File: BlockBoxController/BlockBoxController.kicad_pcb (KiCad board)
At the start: 4 copper layers, 80.5 x 40 mm, 92 parts, among them J1 B1_SWLED, J10 I2C1/USART1, J11 I2C4/UART4, J12 B1_LED_BRIGHTNESS, J13 I2C5, J14 B1_BTN, J15 PWR, J2 SWD, J3 NHD-3.5-320240FT-CON, J4 CHG, J5 AMP, J6 I2S, J7 B1_LCD_SWITCH, J8 LED, J9 B1_LEDMODE, Q1 NX138BK, Q2 NX138BK, Q3 DMG2302UK, Q4 DMG2302UK, Q5 DMG2302UK, Q6 DMG2302UK, U1 STM32H725VGTx

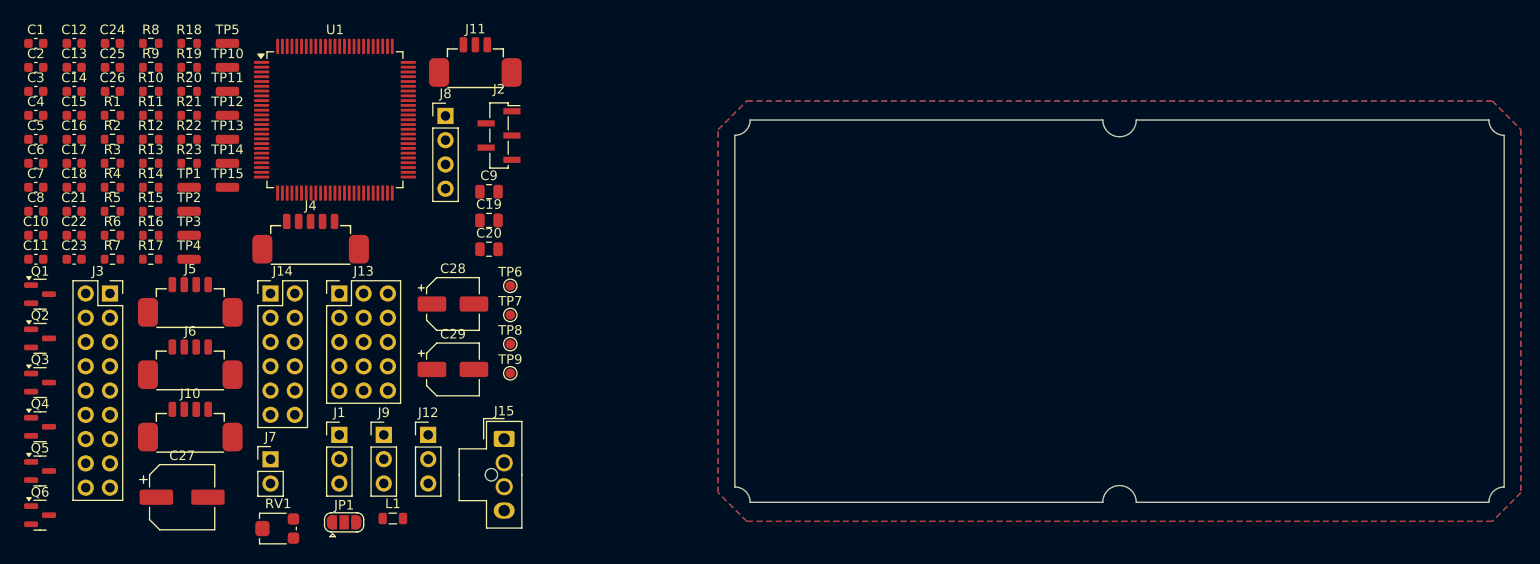
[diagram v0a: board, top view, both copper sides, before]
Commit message: BlockBoxController design done
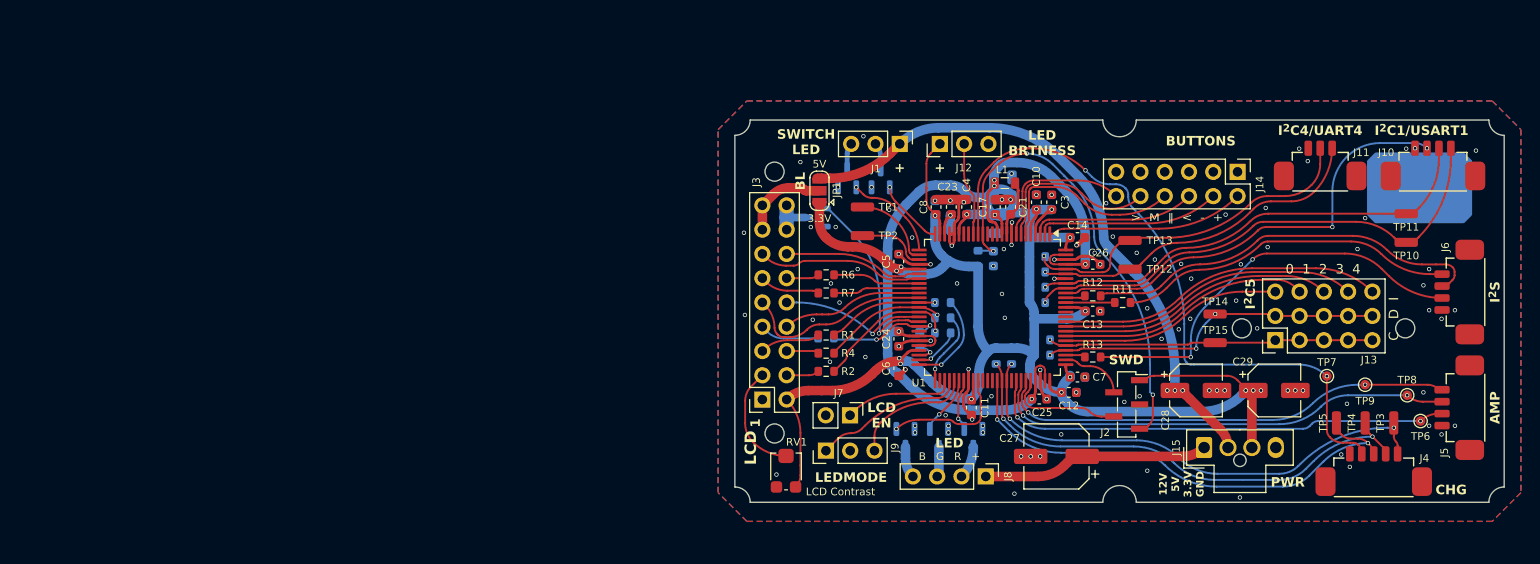
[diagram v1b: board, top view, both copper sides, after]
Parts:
- added REF**: Hole_2mm, BW_PassiveMechanical:Hole_2mm, F.Cu at (113.9, 85.4)
- added REF**: Hole_2mm, BW_PassiveMechanical:Hole_2mm, F.Cu at (179.9, 101.8)
- added REF**: Hole_2mm, BW_PassiveMechanical:Hole_2mm, F.Cu at (162.8, 101.8)
- added REF**: Hole_2mm, BW_PassiveMechanical:Hole_2mm, F.Cu at (113.9, 112.8)
- added REF**: BW_Logo_10x6.4mm, BW_Logo:BW_Logo_10x6.4mm, B.Cu at (181.4, 87.1)
- C1, C15, C16, C18, C19, C2, C20, C22, C9, Q1, Q2, Q3, Q4, Q5, Q6, R10, R14, R15, R16, R17, R18, R19, R20, R21, R22, R23, R3, R5, R8, R9: moved to B.Cu
- moved J5 133.8 mm to (186.2, 110.1), turned to 90 degrees
- moved J6 133.7 mm to (186.2, 98.0), turned to 90 degrees
- moved J10 132.9 mm to (182.8, 85.4)
- moved TP3 127.6 mm to (178.7, 111.7), turned to -90 degrees
- moved TP10 124.7 mm to (180.0, 92.8), turned to 180 degrees
- moved TP4 124.2 mm to (175.7, 111.7), turned to -90 degrees
- moved TP11 124.0 mm to (180.0, 89.8), turned to 180 degrees
- moved TP5 122.7 mm to (172.7, 111.7), turned to -90 degrees
- moved J4 113.9 mm to (176.6, 117.4)
- moved C2 113.3 mm to (144.7, 108.5), turned to 180 degrees
- moved C7 110.8 mm to (145.6, 106.9), turned to 180 degrees
- moved C12 110.3 mm to (144.7, 108.5), turned to 180 degrees
- moved C13 109.6 mm to (147.2, 100.0), turned to 180 degrees
- moved C15 108.5 mm to (145.6, 106.9), turned to 180 degrees
- moved C3 106.9 mm to (142.9, 88.6), turned to -90 degrees
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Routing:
- net +3.3V: track 0.00 -> 196.2 mm, vias 0 -> 17
- net VCC: track 0.00 -> 89.0 mm, vias 0 -> 5
- net /CHG_IOUT: track 0.00 -> 69.0 mm, vias 0 -> 2
- net +5V: track 0.00 -> 65.6 mm, vias 0 -> 3
- net /I2C1_SCL/USART1_TX: track 0.00 -> 52.7 mm, vias 0 -> 1
- net /CHG_SMB_SCL: track 0.00 -> 52.6 mm, vias 0 -> 3
- net /CHG_ACOK: track 0.00 -> 51.9 mm, vias 0 -> 2
- net /CHG_SMB_SDA: track 0.00 -> 51.5 mm, vias 0 -> 3
- net Net-(J2-Pin_5): track 0.00 -> 49.6 mm, vias 0 -> 3
- net /AMP_~{CLIP_OTW}: track 0.00 -> 49.1 mm, vias 0 -> 2
- net /I2C1_SDA/USART1_RX: track 0.00 -> 48.9 mm, vias 0 -> 1
- net /AMP_~{FAULT}: track 0.00 -> 48.8 mm, vias 0 -> 2
- net /AMP_~{RESET}: track 0.00 -> 48.2 mm, vias 0 -> 2
- net /I2C1_~{INT0}: track 0.00 -> 46.5 mm, vias 0 -> 2
- net Net-(J6-Pin_3): track 0.00 -> 43.4 mm, vias 0 -> 2
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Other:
- board text added: "+"
- board text added: "0 1 2 3 4"
- board text added: "1"
- board text added: "12V 5V 3.3V GND"
- board text added: "3.3V"
- board text added: "5V"
- board text added: "> M ‖ < - +"
- board text added: "AMP"
- board text added: "B G R +"
- board text added: "BL"
- board text added: "BUTTONS"
- board text added: "C D I"
- board text added: "CHG"
- board text added: "I^{2}C1/USART1"
- board text added: "I^{2}C4/UART4"
- board text added: "I^{2}C5"
- board text added: "I^{2}S"
- board text added: "LCD"
- board text added: "LCD Contrast"
- board text added: "LCD EN"
- board text added: "LED"
- board text added: "LED BRTNESS"
- board text added: "LEDMODE"
- board text added: "Modular Audio BlockBox Controller"
- board text added: "PWR"
- board text added: "SWD"
- board text added: "SWITCH LED"

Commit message: BlockBoxController minimal firmware
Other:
- board text added: "B R G +"
- board text removed: "B G R +"
